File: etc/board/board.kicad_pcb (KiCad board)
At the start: 2 copper layers, 152.2 x 109.4 mm, 10 parts, among them J1 Conn_01x05, U1 Teensy4.1, U2 BOB-09056, U3 TFT_320x240

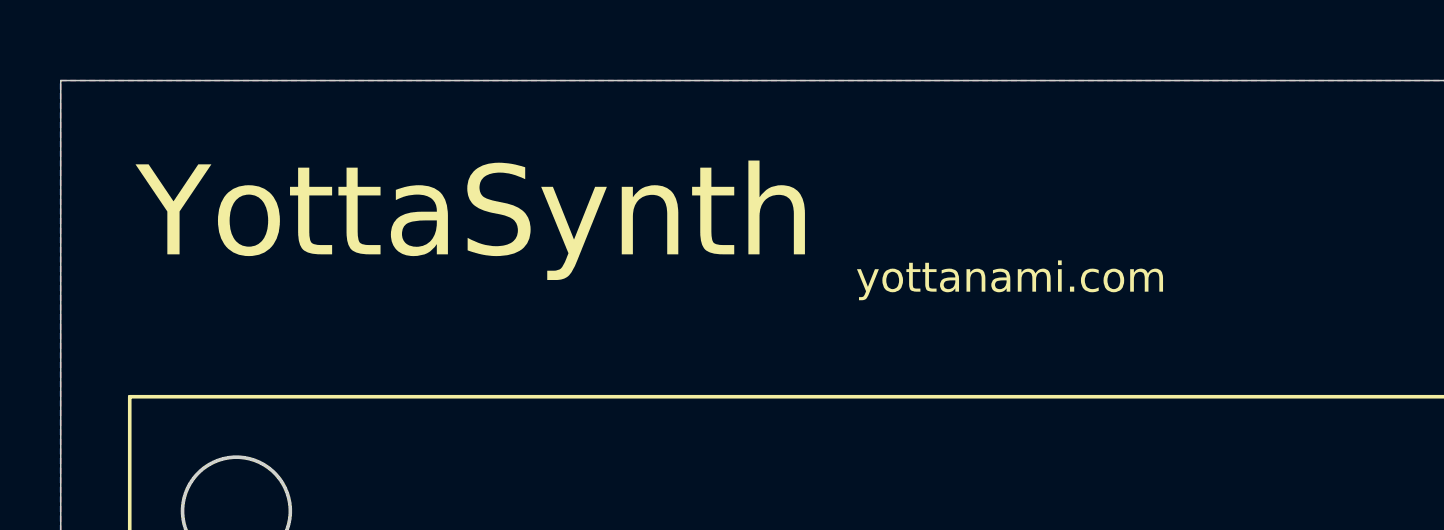
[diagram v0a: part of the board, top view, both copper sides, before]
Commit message: Update board files and scan knob rotates
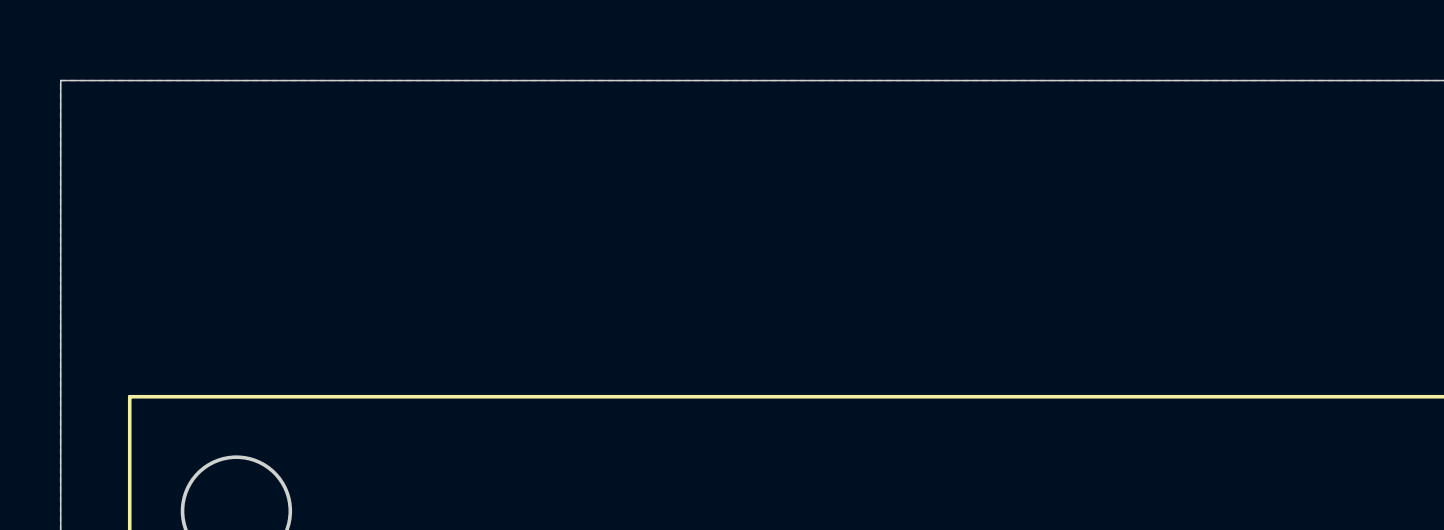
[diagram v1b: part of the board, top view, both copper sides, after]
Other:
- board text removed: "YottaSynth"
- board text removed: "yottanami.com"
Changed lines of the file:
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@@
 		(layer "Edge.Cuts")
-	)
-	(gr_text "yottanami.com"
-		(at 121.5 39 0)
-		(layer "F.SilkS")
-		(effects
-			(font
-				(size 1 1)
-				(thickness 0.1)
-			)
-			(justify left bottom)
-		)
-	)
-	(gr_text "YottaSynth"
-		(at 97.5 38 0)
-		(layer "F.SilkS")
-		(effects
-			(font
-				(size 3 3)
-				(thickness 0.5)
-			)
-			(justify left bottom)
-		)
 	)
 	(segment
